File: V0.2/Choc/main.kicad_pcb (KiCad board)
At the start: 2 copper layers, 127.5 x 87.9 mm, 72 parts

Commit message: V0.2 close to done
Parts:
- removed the S2 at (125.3, 119.3)
- removed the S2 at (89.3, 114.3)
- removed the S2 at (143.3, 95.8)
- removed the S2 at (125.3, 85.3)
- removed the S2 at (125.3, 102.3)
- removed the S2 at (107.3, 97.3)
- removed the S2 at (143.3, 112.8)
- removed the S2 at (179.3, 104.3)
- removed the S2 at (107.3, 131.3)
- removed the S2 at (194.0, 142.6)
- removed the S2 at (161.3, 119.3)
- removed the S2 at (107.3, 114.3)
- removed the S2 at (179.3, 87.3)
- removed the S2 at (153.3, 136.8)
- removed the S2 at (89.3, 131.3)
- removed the S2 at (173.2, 139.4)
- removed the S2 at (179.3, 121.3)
- removed the S2 at (161.3, 102.3)
- removed the S2 at (161.3, 85.3)
- removed the S2 at (143.3, 78.8)
- added S2: , PG1350_Mill_Max:PG1350_Mill_Max, F.Cu at (173.2, 139.4)
- added S2: , PG1350_Mill_Max:PG1350_Mill_Max, F.Cu at (89.3, 131.3)
- added S2: , PG1350_Mill_Max:PG1350_Mill_Max, F.Cu at (125.3, 102.3)
- added S2: , PG1350_Mill_Max:PG1350_Mill_Max, F.Cu at (179.3, 87.3)
- added S2: , PG1350_Mill_Max:PG1350_Mill_Max, F.Cu at (143.3, 95.8)
- added S2: , PG1350_Mill_Max:PG1350_Mill_Max, F.Cu at (194.0, 142.6)
- added S2: , PG1350_Mill_Max:PG1350_Mill_Max, F.Cu at (125.3, 85.3)
- added S2: , PG1350_Mill_Max:PG1350_Mill_Max, F.Cu at (143.3, 112.8)
- added S2: , PG1350_Mill_Max:PG1350_Mill_Max, F.Cu at (153.3, 136.8)
- added S2: , PG1350_Mill_Max:PG1350_Mill_Max, F.Cu at (125.3, 119.3)
- added S2: , PG1350_Mill_Max:PG1350_Mill_Max, F.Cu at (107.3, 97.3)
- added S2: , PG1350_Mill_Max:PG1350_Mill_Max, F.Cu at (161.3, 119.3)
- added S2: , PG1350_Mill_Max:PG1350_Mill_Max, F.Cu at (161.3, 102.3)
- added S2: , PG1350_Mill_Max:PG1350_Mill_Max, F.Cu at (107.3, 131.3)
- added S2: , PG1350_Mill_Max:PG1350_Mill_Max, F.Cu at (161.3, 85.3)
- added S2: , PG1350_Mill_Max:PG1350_Mill_Max, F.Cu at (143.3, 78.8)
- added S2: , PG1350_Mill_Max:PG1350_Mill_Max, F.Cu at (179.3, 104.3)
- added S2: , PG1350_Mill_Max:PG1350_Mill_Max, F.Cu at (89.3, 114.3)
- added S2: , PG1350_Mill_Max:PG1350_Mill_Max, F.Cu at (179.3, 121.3)
- added S2: , PG1350_Mill_Max:PG1350_Mill_Max, F.Cu at (107.3, 114.3)
- S2: footprint PG1350 -> PG1350_Mill_Max:PG1350_Mill_Max
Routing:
- net K6: track 51.6 -> 61.6 mm, vias 0 -> 1

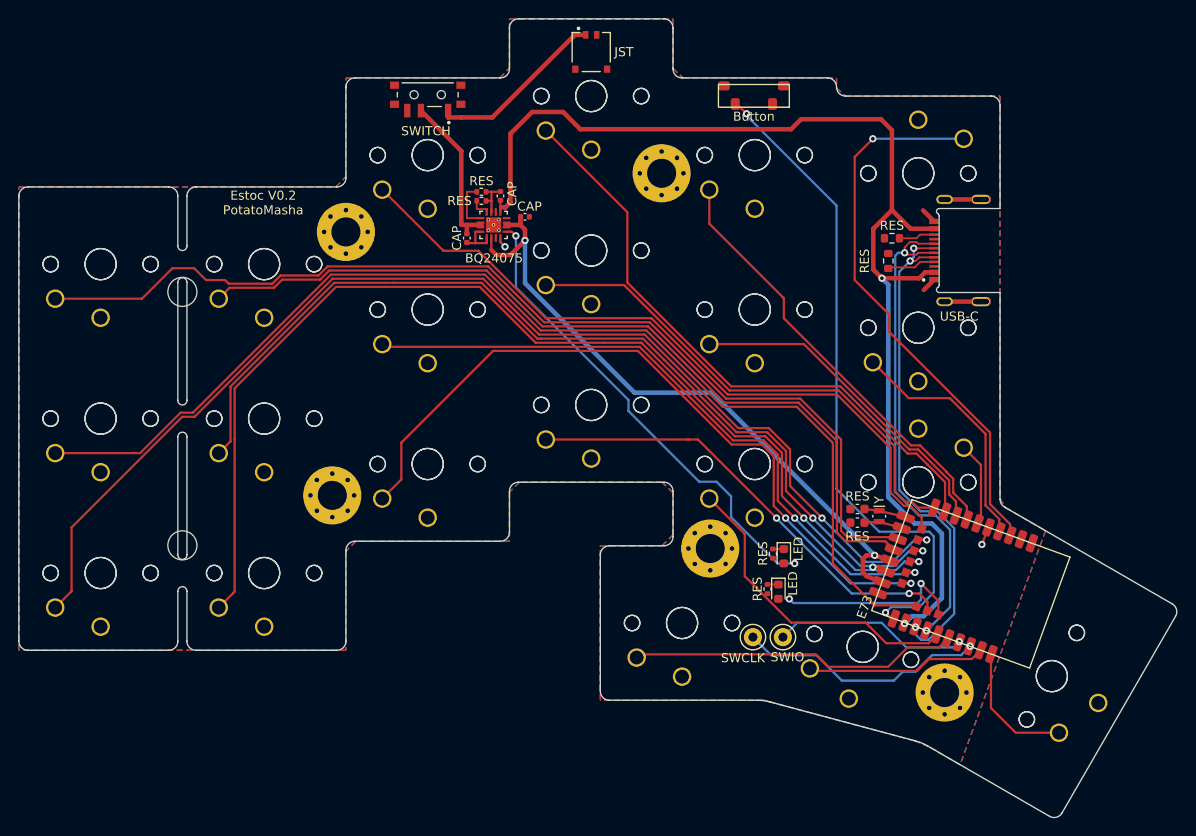
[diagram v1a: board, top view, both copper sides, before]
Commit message: Shrank outline
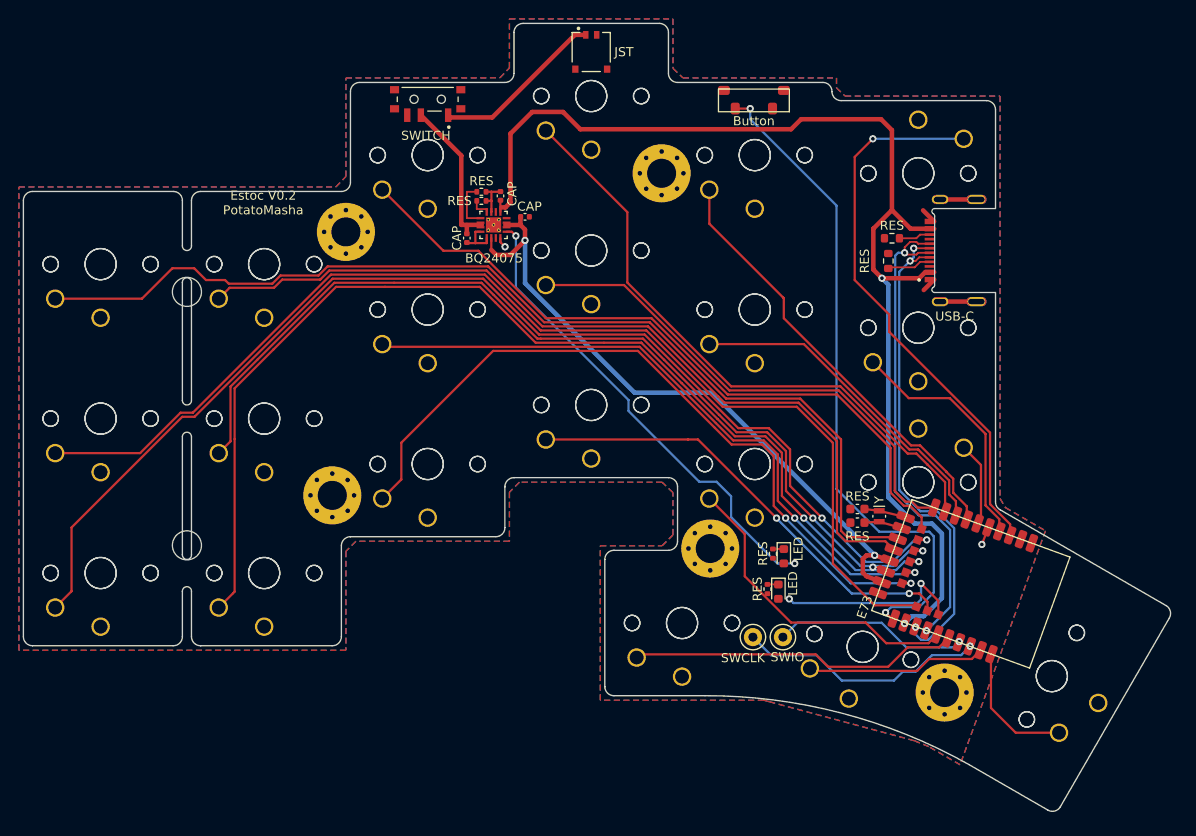
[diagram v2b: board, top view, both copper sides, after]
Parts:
- moved ? 0.50 mm to (181.1, 91.2)
- moved Button 0.50 mm to (165.1, 80.5)
- moved SWITCH 0.50 mm to (125.3, 79.2)
- moved USB-C 0.50 mm to (185.7, 95.8)
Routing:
- net VBAT: track 37.3 -> 36.2 mm
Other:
- board size 127.5 x 87.9 mm -> 126.3 x 86.7 mm

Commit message: Just need to change ESD
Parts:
- removed E73: E73, E73-2G4M08S1E:E73-2G4M08S1E
- removed the RES at (172.6, 125.8)
- removed the RES at (172.6, 124.2)
- removed SWCLK, SWIO: TestPoint_Keystone_5000-5004_Miniature, TestPoint:TestPoint_Keystone_5000-5004_Miniature
- removed Y: Y1, Crystal:Crystal_SMD_MicroCrystal_CM9V-T1A-2Pin_1.6x1.0mm
- added 0: MountingHole_3.2mm_M3_Pad_Via, MountingHole:MountingHole_3.2mm_M3_Pad_Via, B.Cu at (271.9, 110.2)
- added ?: , clipboard:8583f098-8525-47d3-99c4-a63cf4c513a4, B.Cu at (205.6, 78.6)
- added ?: , , F.Cu at (206.8, 136.2)
- added ?: , , F.Cu at (203.6, 137.4)
- added ?: , , F.Cu at (149.2, 106.3)
- added ?: , , F.Cu at (208.4, 135.6)
- added ?: , , F.Cu at (205.2, 136.8)
- added ?: , , F.Cu at (149.2, 104.6)
- added ?: , , F.Cu at (149.2, 102.9)
- added ?: , , F.Cu at (149.2, 101.2)
- added BQ24075: BQ24075, BQ24075TRGTT:QFN50P300X300X100-17N, B.Cu at (248.4, 76.7)
- added Button: TL3330AF260QG, TL3330AF260QG:TL3330AF260QG, F.Cu at (229.4, 68.0)
- added CAP: CAP, Capacitor_SMD:C_0402_1005Metric, B.Cu at (247.7, 73.5)
- added CAP: CAP, Capacitor_SMD:C_0402_1005Metric, B.Cu at (251.4, 78.1)
- added CAP: CAP, Capacitor_SMD:C_0402_1005Metric, B.Cu at (245.0, 75.8)
- added JST: JST_BM02B, BM02B-ACHSS-GAN-TF_LF__SN_:JST_BM02B-ACHSS-GAN-TF(LF)(SN), F.Cu at (243.4, 61.4)
- added LED: LED, LED_SMD:LED_0603_1608Metric, B.Cu at (222.2, 116.9)
- added LED: LED, LED_SMD:LED_0603_1608Metric, B.Cu at (222.8, 120.8)
- added REF**: MountingHole_3.2mm_M3, MountingHole:MountingHole_3.2mm_M3, B.Cu at (288.4, 115.7)
- added REF**: MountingHole_3.2mm_M3_Pad_Via, MountingHole:MountingHole_3.2mm_M3_Pad_Via, B.Cu at (204.5, 131.9)
- added REF**: MountingHole_3.2mm_M3_Pad_Via, MountingHole:MountingHole_3.2mm_M3_Pad_Via, B.Cu at (270.4, 81.2)
- added REF**: MountingHole_3.2mm_M3_Pad_Via, MountingHole:MountingHole_3.2mm_M3_Pad_Via, B.Cu at (230.3, 116.1)
- added REF**: MountingHole_3.2mm_M3, MountingHole:MountingHole_3.2mm_M3, B.Cu at (288.4, 87.8)
- added REF**: Hole, MountingHole:MountingHole_3.2mm_M3_Pad_Via, B.Cu at (235.7, 74.8)
- added RES: RES, Resistor_SMD:R_0402_1005Metric, B.Cu at (249.8, 73.0)
- added RES: RES, Resistor_SMD:R_0603_1608Metric, B.Cu at (210.3, 81.9)
- added RES: RES, Resistor_SMD:R_0402_1005Metric, B.Cu at (249.8, 74.0)
- added RES: RES, Resistor_SMD:R_0603_1608Metric, B.Cu at (210.7, 84.4)
- added RES: RES, Resistor_SMD:R_0402_1005Metric, B.Cu at (223.4, 116.6)
- added RES: RES, Resistor_SMD:R_0402_1005Metric, B.Cu at (224.0, 120.5)
- added S1: , PG1350, B.Cu at (279.4, 101.8)
- added S1: , PG1350, B.Cu at (243.4, 83.3)
- added S1: , PG1350, B.Cu at (261.4, 72.8)
- added S1: , PG1350, B.Cu at (213.5, 126.9)
- added S1: , PG1350, B.Cu at (233.4, 124.3)
- added S1: , PG1350, B.Cu at (243.4, 100.3)
- added S1: , PG1350, B.Cu at (243.4, 66.3)
- added S1: , PG1350, B.Cu at (207.4, 74.8)
- added S1: , PG1350, B.Cu at (207.4, 91.8)
- added S1: , PG1350, B.Cu at (261.4, 89.8)
- added S1: , PG1350, B.Cu at (297.4, 101.8)
- added S1: , PG1350, B.Cu at (279.4, 84.8)
- added S1: , PG1350, B.Cu at (192.7, 130.1)
- added S1: , PG1350, B.Cu at (279.4, 118.8)
- added S1: , PG1350, B.Cu at (225.4, 106.8)
- added S1: , PG1350, B.Cu at (297.4, 118.8)
- added S1: , PG1350, B.Cu at (297.4, 84.8)
- added S1: , PG1350, B.Cu at (225.4, 89.8)
- added S1: , PG1350, B.Cu at (225.4, 72.8)
- added S1: , PG1350, B.Cu at (207.4, 108.8)
- added S1: , PG1350, B.Cu at (261.4, 106.8)
- added S2: , PG1350_Mill_Max:PG1350_Mill_Max, B.Cu at (279.4, 118.8)
- added S2: , PG1350_Mill_Max:PG1350_Mill_Max, B.Cu at (261.4, 89.8)
- added S2: , PG1350_Mill_Max:PG1350_Mill_Max, B.Cu at (225.4, 89.8)
- added S2: , PG1350_Mill_Max:PG1350_Mill_Max, B.Cu at (192.7, 130.1)
- added S2: , PG1350_Mill_Max:PG1350_Mill_Max, B.Cu at (213.5, 126.9)
- added S2: , PG1350_Mill_Max:PG1350_Mill_Max, B.Cu at (261.4, 106.8)
- added S2: , PG1350_Mill_Max:PG1350_Mill_Max, B.Cu at (243.4, 100.3)
- added S2: , PG1350_Mill_Max:PG1350_Mill_Max, B.Cu at (225.4, 106.8)
- added S2: , PG1350_Mill_Max:PG1350_Mill_Max, B.Cu at (233.4, 124.3)
- added S2: , PG1350_Mill_Max:PG1350_Mill_Max, B.Cu at (279.4, 101.8)
- added S2: , PG1350_Mill_Max:PG1350_Mill_Max, B.Cu at (279.4, 84.8)
- added S2: , PG1350_Mill_Max:PG1350_Mill_Max, B.Cu at (207.4, 91.8)
- added S2: , PG1350_Mill_Max:PG1350_Mill_Max, B.Cu at (297.4, 101.8)
- added S2: , PG1350_Mill_Max:PG1350_Mill_Max, B.Cu at (207.4, 108.8)
- added S2: , PG1350_Mill_Max:PG1350_Mill_Max, B.Cu at (243.4, 83.3)
- added S2: , PG1350_Mill_Max:PG1350_Mill_Max, B.Cu at (243.4, 66.3)
- added S2: , PG1350_Mill_Max:PG1350_Mill_Max, B.Cu at (297.4, 84.8)
- added S2: , PG1350_Mill_Max:PG1350_Mill_Max, B.Cu at (297.4, 118.8)
- added S2: , PG1350_Mill_Max:PG1350_Mill_Max, B.Cu at (225.4, 72.8)
- added S2: , PG1350_Mill_Max:PG1350_Mill_Max, B.Cu at (207.4, 74.8)
- added S2: , PG1350_Mill_Max:PG1350_Mill_Max, B.Cu at (261.4, 72.8)
- added SWITCH: SW_EG1215AA, EG1215AA:SW_EG1215AA, F.Cu at (261.4, 66.6)
- added USB-C: USB-C, 2169900003:MOLEX_2169900003, F.Cu at (201.0, 83.3)
- added nRF52833: MS88SF3_Min, 0_ARognes:MS88SF3_Min, F.Cu at (201.6, 120.4)
- added nRF52833: MS88SF3_Min, 0_ARognes:MS88SF3_Min, F.Cu at (147.8, 120.6)
- S1 (x21), S2 (x21): moved to B.Cu
- moved S1 39.3 mm to (142.0, 75.0), turned to 0 degrees
- moved S1 39.3 mm to (142.0, 109.0), turned to 0 degrees
- moved S1 39.3 mm to (142.0, 92.0), turned to 180 degrees
- moved S2 39.3 mm to (142.0, 92.0), turned to 0 degrees
- moved S2 39.3 mm to (142.0, 109.0), turned to 180 degrees
- moved S2 39.3 mm to (142.0, 75.0), turned to 180 degrees
- moved JST 39.3 mm to (106.0, 61.6)
- moved LED 39.3 mm to (126.6, 121.0)
- moved REF** 39.3 mm to (119.1, 116.3)
- moved REF** 39.3 mm to (113.7, 75.0)
- moved RES 39.3 mm to (126.0, 116.8)
- moved S1 39.3 mm to (106.0, 66.5), turned to 180 degrees
- moved S1 39.3 mm to (116.0, 124.5), turned to 180 degrees
- moved S1 39.3 mm to (124.0, 73.0), turned to 180 degrees
- moved S1 39.3 mm to (124.0, 107.0), turned to 180 degrees
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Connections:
- LED pad 2: VDDH -> STATUS
- LED pad 2: VDDH -> CHG
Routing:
- net K13: track 132.3 -> 0.00 mm
- net K7: track 125.9 -> 0.00 mm
- net K14: track 122.2 -> 0.00 mm
- net K1: track 113.9 -> 0.00 mm
- net K8: track 106.0 -> 0.00 mm
- net K2: track 94.2 -> 0.00 mm
- net K15: track 82.1 -> 0.00 mm
- net K9: track 73.2 -> 0.00 mm
- net K4: track 67.8 -> 0.00 mm
- net K3: track 78.5 -> 12.6 mm
- net K6: track 61.6 -> 0.00 mm, vias 1 -> 0
- net K10: track 55.8 -> 0.00 mm
- net K16: track 50.4 -> 0.00 mm
- net K5: track 48.6 -> 0.00 mm
- net K11: track 36.8 -> 0.00 mm
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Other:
- board size 126.3 x 86.7 mm -> 262.5 x 87 mm

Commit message: Difficult circuitry complete, just wire
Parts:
- added U1: SOT-457, IP4234CZ6:SOT-457, F.Cu at (139.1, 88.9)
- moved ? 1.00 mm to (148.2, 106.3)
- moved ? 1.00 mm to (148.2, 104.6)
- moved ? 1.00 mm to (148.2, 102.9)
- moved ? 1.00 mm to (148.2, 101.2)
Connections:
- ? pad : SWCLK -> SWIO
- ? pad : SWIO -> SWCLK
- ? pad : VDDH -> GND
- ? pad : GND -> VDDH
- nRF52833 pad 1 GND: (no net) -> GND
- nRF52833 pad 18 GND: (no net) -> GND
- nRF52833 pad 34 GND: (no net) -> GND
- nRF52833 pad 35 VBUS: (no net) -> VBUS
- nRF52833 pad 36 D-: D- -> D-ESD
- nRF52833 pad 37 D+: D+ -> D+ESD
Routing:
- net D-ESD: track 0.00 -> 28.8 mm
- net D+ESD: track 0.00 -> 25.9 mm
- net D-: track 34.5 -> 12.9 mm, vias 5 -> 6
- net D+: track 36.1 -> 16.3 mm, vias 3 -> 4
- net VBUS: track 101.7 -> 109.3 mm, vias 3 -> 2
- net SWCLK: track 24.7 -> 28.6 mm

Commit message: Left half complete
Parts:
- moved CAP 0.55 mm to (104.9, 75.8)
- moved 0 0.35 mm to (77.8, 110.5)
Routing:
- net K13: track 0.00 -> 105.0 mm, vias 2 -> 1
- net K1: track 0.00 -> 103.2 mm
- net K7: track 0.00 -> 98.7 mm
- net K14: track 0.00 -> 86.5 mm, vias 2 -> 1
- net K8: track 0.00 -> 78.1 mm, vias 2 -> 1
- net K2: track 0.00 -> 77.1 mm
- net K3: track 12.6 -> 84.4 mm
- net K15: track 0.00 -> 63.3 mm, vias 2 -> 1
- net K4: track 0.00 -> 59.5 mm, vias 0 -> 1
- net K9: track 0.00 -> 57.2 mm, vias 2 -> 1
- net K6: track 0.00 -> 53.3 mm, vias 0 -> 1
- net K5: track 0.00 -> 45.7 mm, vias 0 -> 1
- net K10: track 0.00 -> 43.0 mm
- net K16: track 0.00 -> 42.1 mm, vias 2 -> 1
- net K19: track 0.00 -> 28.6 mm
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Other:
- board text added: "Gravi V0.2 PotatoBoards"

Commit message: Fix curve issues
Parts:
- removed the 0 at (271.9, 110.2)
- removed the ? at (205.6, 78.6)
- removed the ? at (206.8, 136.2)
- removed the ? at (203.6, 137.4)
- removed the ? at (208.4, 135.6)
- removed the ? at (205.2, 136.8)
- removed the BQ24075 at (248.4, 76.7)
- removed the Button at (229.4, 68.0)
- removed the CAP at (247.7, 73.5)
- removed the CAP at (251.4, 78.1)
- removed the CAP at (245.0, 75.8)
- removed the JST at (243.4, 61.4)
- removed the LED at (222.2, 116.9)
- removed the LED at (222.8, 120.8)
- removed the REF** at (288.4, 115.7)
- removed the REF** at (204.5, 131.9)
- removed the REF** at (270.4, 81.2)
- removed the REF** at (230.3, 116.1)
- removed the REF** at (288.4, 87.8)
- removed the REF** at (235.7, 74.8)
- removed the RES at (249.8, 73.0)
- removed the RES at (210.3, 81.9)
- removed the RES at (249.8, 74.0)
- removed the RES at (210.7, 84.4)
- removed the RES at (223.4, 116.6)
- removed the RES at (224.0, 120.5)
- removed the S1 at (279.4, 101.8)
- removed the S1 at (106.0, 66.5)
- removed the S1 at (243.4, 83.3)
- removed the S1 at (261.4, 72.8)
- removed the S1 at (213.5, 126.9)
- removed the S1 at (233.4, 124.3)
- removed the S1 at (243.4, 100.3)
- removed the S1 at (243.4, 66.3)
- removed the S1 at (207.4, 74.8)
- removed the S1 at (207.4, 91.8)
- removed the S1 at (261.4, 89.8)
- removed the S1 at (297.4, 101.8)
- removed the S1 at (279.4, 84.8)
- removed the S1 at (192.7, 130.1)
- removed the S1 at (279.4, 118.8)
- removed the S1 at (225.4, 106.8)
- removed the S1 at (297.4, 118.8)
- removed the S1 at (297.4, 84.8)
- removed the S1 at (225.4, 89.8)
- removed the S1 at (225.4, 72.8)
- removed the S1 at (207.4, 108.8)
- removed the S1 at (261.4, 106.8)
- removed the S2 at (279.4, 118.8)
- removed the S2 at (261.4, 89.8)
- removed the S2 at (225.4, 89.8)
- removed the S2 at (192.7, 130.1)
- removed the S2 at (213.5, 126.9)
- removed the S2 at (261.4, 106.8)
- removed the S2 at (243.4, 100.3)
- removed the S2 at (225.4, 106.8)
- removed the S2 at (233.4, 124.3)
- removed the S2 at (279.4, 101.8)
- removed the S2 at (279.4, 84.8)
- removed the S2 at (207.4, 91.8)
- removed the S2 at (297.4, 101.8)
- removed the S2 at (207.4, 108.8)
- removed the S2 at (243.4, 83.3)
- removed the S2 at (243.4, 66.3)
- removed the S2 at (297.4, 84.8)
- removed the S2 at (297.4, 118.8)
- removed the S2 at (225.4, 72.8)
- removed the S2 at (207.4, 74.8)
- removed the S2 at (261.4, 72.8)
- removed the SWITCH at (261.4, 66.6)
- removed the USB-C at (201.0, 83.3)
- removed the nRF52833 at (201.6, 120.4)
- added G***: LOGO, LOGO, F.Cu at (166.4, 97.5)
- added G***: LOGO, LOGO, B.Cu at (178.9, 120.2)
- added G***: LOGO, LOGO, B.Cu at (132.4, 68.0)
- added G***: LOGO, LOGO, B.Cu at (233.8, 126.8)
- added G***: LOGO, LOGO, B.Cu at (201.8, 89.4)
- added G***: LOGO, LOGO, B.Cu at (153.1, 107.5)
- added G***: LOGO, LOGO, B.Cu at (158.5, 59.4)
- added G***: LOGO, LOGO, B.Cu at (173.4, 106.3)
- added G***: LOGO, LOGO, B.Cu at (186.6, 63.1)
- added G***: LOGO, LOGO, B.Cu at (119.0, 111.4)
- added G***: LOGO, LOGO, B.Cu at (140.0, 122.2)
- added G***: LOGO, LOGO, B.Cu at (109.6, 97.8)
- added G***: LOGO, LOGO, B.Cu at (202.4, 140.3)
- added G***: LOGO, LOGO, B.Cu at (208.5, 107.1)
- added S1: , PG1350, B.Cu at (166.1, 65.9)
- moved CAP 60.1 mm to (161.9, 73.1)
- moved LED 60.1 mm to (187.3, 116.5)
- moved ? 60.1 mm to (203.9, 78.3)
- moved ? 60.1 mm to (208.3, 105.7)
- moved ? 60.1 mm to (208.3, 104.0)
- moved ? 60.1 mm to (208.3, 102.3)
- moved ? 60.1 mm to (208.3, 100.6)
- moved Button 60.1 mm to (187.9, 67.6)
- moved CAP 60.1 mm to (165.1, 75.2)
- moved REF** 60.1 mm to (205.0, 131.6)
- moved RES 60.1 mm to (198.8, 84.0)
- moved RES 60.1 mm to (185.5, 120.2)
- moved S1 60.1 mm to (202.1, 108.4)
- moved S1 60.1 mm to (202.1, 91.4)
- moved S1 60.1 mm to (202.1, 74.4)
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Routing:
- net SWIO: track 27.0 -> 12.6 mm
- net SWCLK: track 28.6 -> 14.8 mm
- net GND: track 25.4 -> 11.8 mm, vias 2 -> 1
- net VDDH: track 76.4 -> 85.9 mm
- net K3: track 84.4 -> 76.6 mm
- net VBAT: track 45.0 -> 39.0 mm
- net VBUS: track 109.5 -> 103.8 mm, vias 2 -> 0
- net (no net): track 17.1 -> 11.6 mm
- net K13: track 105.0 -> 100.7 mm, vias 1 -> 0
- net CHG: track 57.3 -> 53.6 mm, vias 4 -> 2
- net K14: track 86.5 -> 83.7 mm, vias 1 -> 0
- net K7: track 98.7 -> 96.3 mm
- net D-: track 12.9 -> 10.7 mm, vias 6 -> 3
- net K1: track 103.2 -> 101.0 mm
- net K8: track 78.1 -> 76.2 mm, vias 1 -> 0
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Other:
- board size 262.5 x 87 mm -> 126.3 x 86.7 mm
